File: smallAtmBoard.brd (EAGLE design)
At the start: 66.1 x 51.7 mm, 26 parts, among them IC1 ATMEGA-328P, IC2 7805-V, Y1 16MHz

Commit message: Idioten schriftzug
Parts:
- added U$6: (no value), bauteile_jbt:SOLDER
- added U$7: (no value), bauteile_jbt:COMP
- moved PAD6 2.54 mm to (11.4, 6.35)
- flipped R23 to the bottom
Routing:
- net GND: track 65.3 -> 60.3 mm, vias 12 -> 6
- net N$26: track 7.72 -> 10.1 mm

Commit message: docu, finetuning
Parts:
- moved U$6 3.33 mm to (11.3, 2.67), turned to 180 degrees
- moved U$7 3.06 mm to (11.2, 2.67), turned to 0 degrees
- moved R3 0.85 mm to (63.4, 37.4)
- moved C5 0.38 mm to (54.5, 48.9)
- moved C4 0.28 mm to (47.3, 48.9)
- moved R16 0.13 mm to (61.8, 48.7)
- moved SV2 0.13 mm to (43.3, 35.6)
- moved SV3 0.13 mm to (43.3, 17.8)
- moved S4 0.13 mm to (51.7, 4.83)
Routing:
- net GND: track 60.3 -> 52.5 mm, vias 6 -> 5
- net N$26: track 10.1 -> 8.57 mm
- net VCC: track 149.7 -> 148.5 mm
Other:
- outline, holes or cut-outs redrawn
- board text added: "(c) jbenoit 2018"

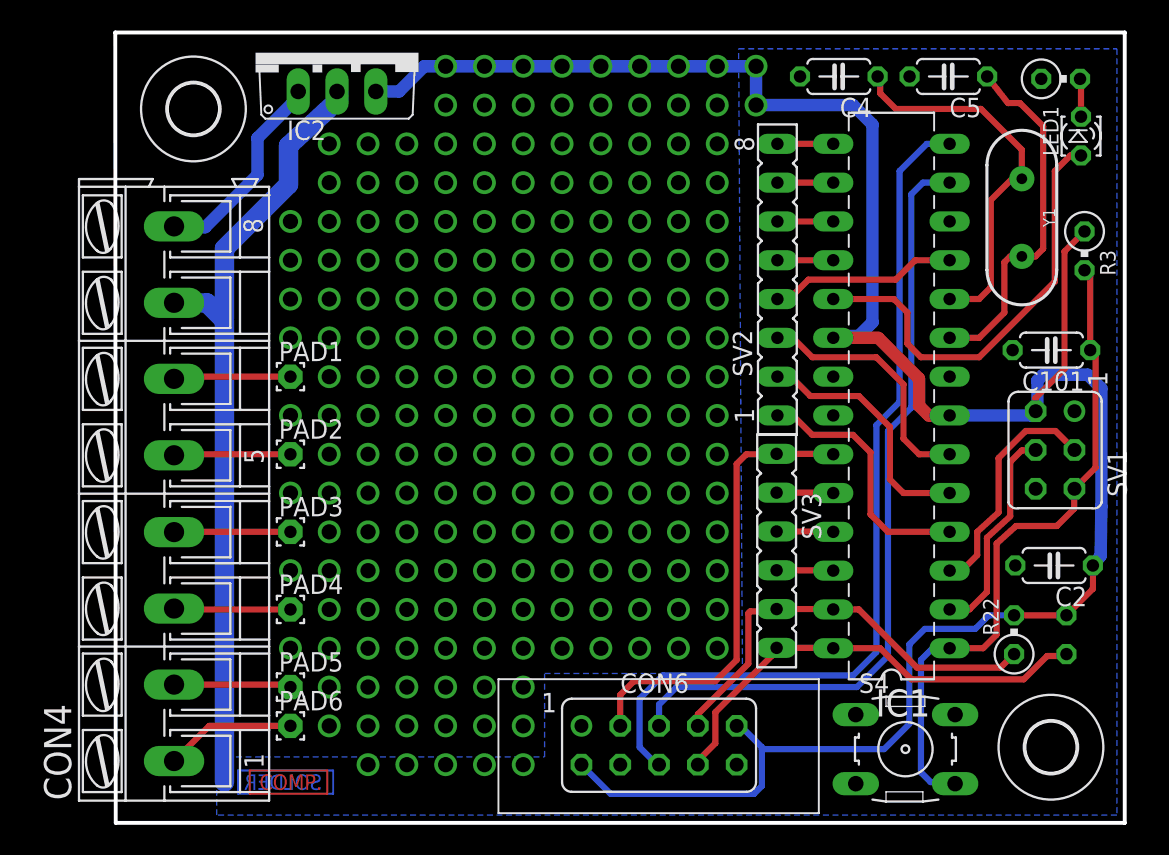
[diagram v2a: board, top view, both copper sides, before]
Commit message: fix grid and value positioning
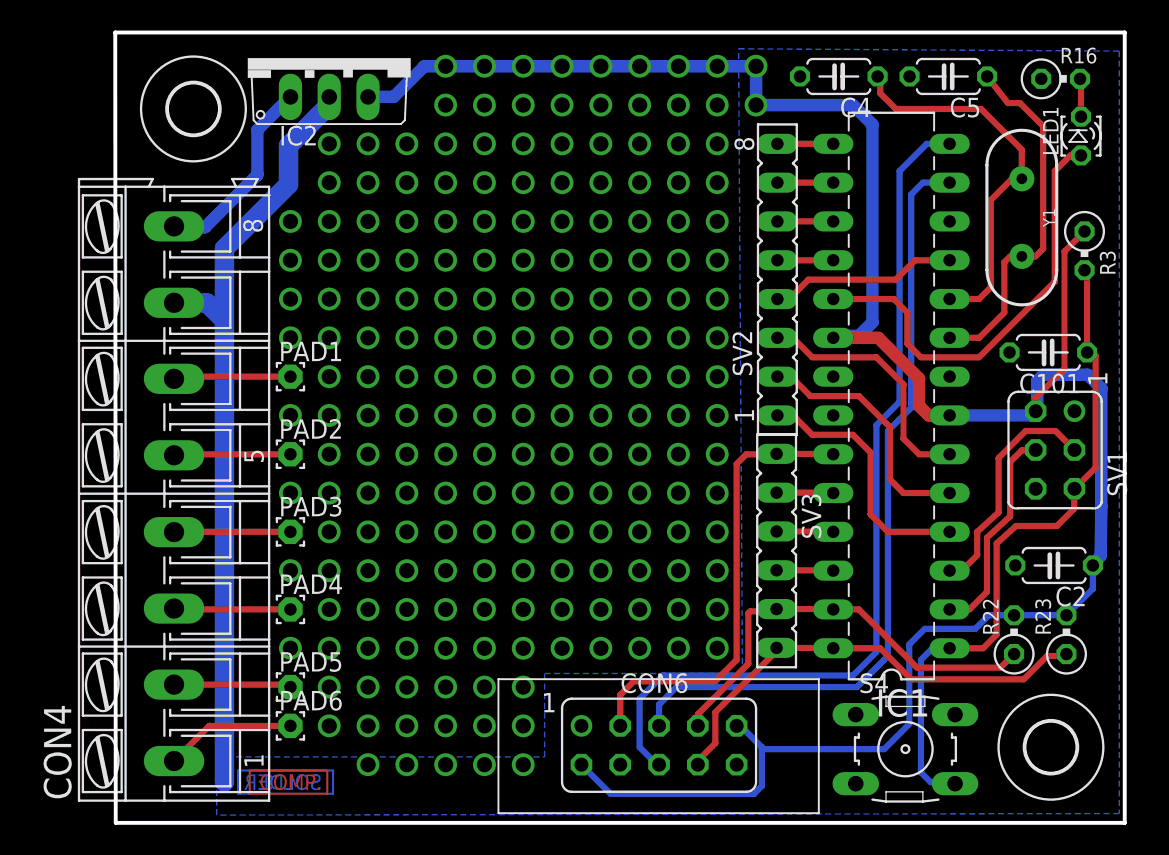
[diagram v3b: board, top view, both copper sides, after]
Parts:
- moved IC2 0.62 mm to (14.0, 50.1)
- moved C101 0.25 mm to (61.0, 30.8)
- flipped R23 to the top
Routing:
- net GND: track 52.5 -> 51.7 mm
- net VCC: track 148.5 -> 149.2 mm
- net +12V: track 13.5 -> 12.9 mm
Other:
- board text added: "jbenoit 2018"
- board text removed: "(c) jbenoit 2018"

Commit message: new connectors + routing
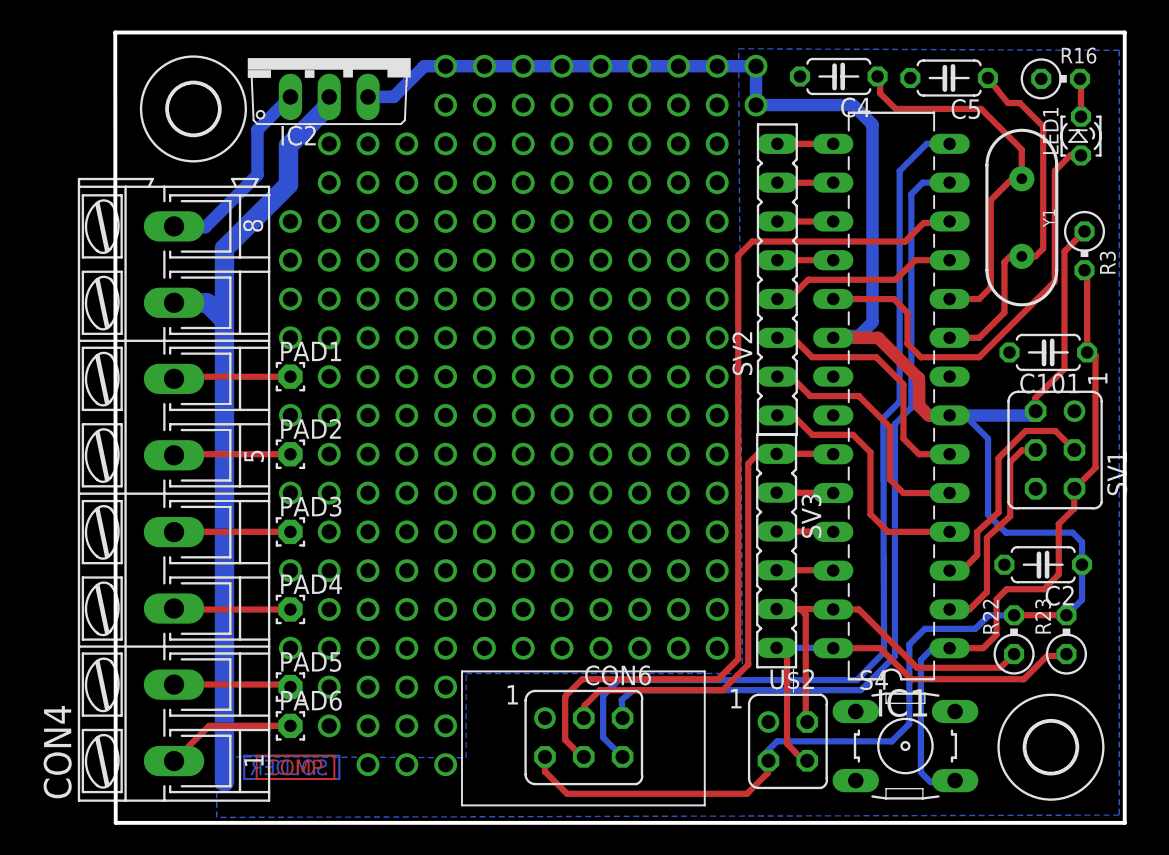
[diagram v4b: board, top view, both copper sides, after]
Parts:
- added U$2: FE02-2, bauteile_jbt:FE02-2RAW
- CON6: device bauteile_jbt:FE05-2 -> bauteile_jbt:FE03-2
- SV2: device con-lsta:FE08 -> bauteile_jbt:FE08
- moved CON6 4.95 mm to (30.6, 5.59)
- moved U$7 1.07 mm to (11.6, 3.63)
- moved U$6 1.05 mm to (11.7, 3.63)
- moved C2 0.71 mm to (60.7, 16.9)
- moved S4 0.20 mm to (51.7, 5.03)
- moved C5 0.11 mm to (54.5, 48.8)
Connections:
- net AT-A4/SDA: now also U$2.3; no longer CON6.7
- net AT-A5/SCL: now also U$2.4; no longer CON6.8
- net AT-PD6: now also CON6.4
- net GND: now also U$2.1; no longer CON6.10
- net VCC: now also U$2.2; no longer CON6.9
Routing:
- net AT-PD6: track 0.00 -> 58.0 mm
- net AT-A4/SDA: track 28.2 -> 25.1 mm
- net VCC: track 149.2 -> 146.3 mm
- net AT-PD7: track 51.4 -> 53.7 mm
- net AT-PD8: track 57.8 -> 60.1 mm
- net AT-A0: track 30.0 -> 31.7 mm
- net AT-A5/SCL: track 30.4 -> 28.9 mm
- net GND: vias 5 -> 3
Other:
- board text added: "12"
- board text added: "3"
- board text added: "4"
- board text added: "5"
- board text added: "D6"
- board text added: "I2C"
- board text added: "LCD/KBD"
- board text added: "github.com/benoitjoh 2018"
- board text removed: "jbenoit 2018"

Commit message: adjust to new system and gerbmerge
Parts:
- moved CON6 1.23 mm to (31.8, 5.08)
- moved U$2 0.85 mm to (43.2, 5.08)
- moved S4 0.38 mm to (52.1, 5.03)
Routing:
- net VCC: track 146.3 -> 144.3 mm
- net AT-A0: track 31.7 -> 30.9 mm
- net AT-PD8: track 60.1 -> 59.3 mm
- net AT-PD6: track 58.0 -> 57.4 mm
- net AT-PD7: track 53.7 -> 53.1 mm
- net AT-A5/SCL: track 28.9 -> 29.4 mm
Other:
- board text added: "+"
- board text removed: "+12V"
